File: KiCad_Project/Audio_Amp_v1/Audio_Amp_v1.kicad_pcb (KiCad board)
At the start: 2 copper layers, 93.5 x 52.8 mm, 61 parts, among them IC2 TPA3116D2DAD, IC4 LMR33630ADDA, J1 TS-103-T-A, J2 1729128, J3 1729128, J4 PJ-102AH

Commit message: Started routing
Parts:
- removed CHF1: 220n, Capacitor_SMD:C_0805_2012Metric
- removed CIN1: 10u, Capacitor_SMD:C_1206_3216Metric
- removed IC4: LMR33630ADDA, LMR33630:SOIC127P600X170-9N
- removed J4: PJ-102AH, 24V-JACK:PJ-102AH
- removed L5: IHLP2525CZER6R8M8A, IHLP2525CZER6R8M8A:INDPM6965X300N
- removed R3: 100k, Resistor_SMD:R_0603_1608Metric
- added C30: 10u, Capacitor_SMD:C_0805_2012Metric, F.Cu at (86.8, 96.9)
- added C31: 1u, Capacitor_SMD:C_0603_1608Metric, F.Cu at (101.0, 89.5)
- added C32: 1u, Capacitor_SMD:C_0603_1608Metric, F.Cu at (101.3, 93.1)
- added C33: 1u, Capacitor_SMD:C_0603_1608Metric, F.Cu at (101.3, 96.1)
- added C34: 10u, Capacitor_SMD:C_0603_1608Metric, F.Cu at (101.3, 94.6)
- added C35: 33p, Capacitor_SMD:C_0603_1608Metric, F.Cu at (88.0, 87.9)
- added C36: 33p, Capacitor_SMD:C_0603_1608Metric, F.Cu at (101.0, 87.8)
- added C37: 1u, Capacitor_SMD:C_0603_1608Metric, F.Cu at (88.8, 96.6)
- added C38: 10u, Capacitor_SMD:CP_Elec_4x5.8, F.Cu at (98.0, 101.1)
- added C39: 470u, Capacitor_SMD:CP_Elec_10x10.5, F.Cu at (117.2, 93.0)
- added C40: 10u, Capacitor_SMD:CP_Elec_4x5.8, F.Cu at (91.0, 101.1)
- added C41: 470u, Capacitor_SMD:CP_Elec_10x10.5, F.Cu at (117.5, 120.5)
- added C42: 10u, Capacitor_SMD:C_0805_2012Metric, F.Cu at (79.0, 120.0)
- added C45: 10u, Capacitor_SMD:C_0805_2012Metric, F.Cu at (81.8, 114.2)
- added C50: 100n, Capacitor_SMD:C_0603_1608Metric, F.Cu at (96.8, 122.5)
- added C51: 10u, Capacitor_SMD:C_0805_2012Metric, F.Cu at (96.8, 125.2)
- added C52: 100n, Capacitor_SMD:C_1206_3216Metric, F.Cu at (102.4, 115.5)
- added C53: 100n, Capacitor_SMD:C_1206_3216Metric, F.Cu at (105.2, 115.5)
- added C54: 100n, Capacitor_SMD:C_1206_3216Metric, F.Cu at (87.8, 115.4)
- added C55: 100n, Capacitor_SMD:C_1206_3216Metric, F.Cu at (90.6, 115.4)
- added C56: 10u, Capacitor_SMD:CP_Elec_4x5.8, F.Cu at (100.5, 126.2)
- added C57: 10u, Capacitor_SMD:CP_Elec_4x5.8, F.Cu at (93.0, 126.2)
- added C59: 2n2, Capacitor_SMD:C_0603_1608Metric, F.Cu at (88.3, 121.7)
- added C62: 2n2, Capacitor_SMD:C_0603_1608Metric, F.Cu at (91.3, 121.7)
- added C63: 2n2, Capacitor_SMD:C_0603_1608Metric, F.Cu at (102.3, 121.8)
- added C64: 2n2, Capacitor_SMD:C_0603_1608Metric, F.Cu at (105.3, 121.8)
- added H1: MountingHole_Pad, MountingHole:MountingHole_3.2mm_M3_Pad_Via, F.Cu at (159.0, 82.8)
- added H2: MountingHole_Pad, MountingHole:MountingHole_3.2mm_M3_Pad_Via, F.Cu at (159.0, 135.8)
- added H3: MountingHole_Pad, MountingHole:MountingHole_3.2mm_M3_Pad_Via, F.Cu at (68.0, 135.8)
- added H4: MountingHole_Pad, MountingHole:MountingHole_3.2mm_M3_Pad_Via, F.Cu at (68.0, 82.8)
- added J6: USB_C_Receptacle_USB2.0_16P, Connector_USB:USB_C_Receptacle_GCT_USB4105-xx-A_16P_TopMnt_Horizontal, F.Cu at (66.3, 93.2)
- added Q2: BSS138, Package_TO_SOT_SMD:SOT-23, F.Cu at (106.2, 90.8)
- added R10: 22, Resistor_SMD:R_0603_1608Metric, F.Cu at (87.9, 92.0)
- added R11: 22, Resistor_SMD:R_0603_1608Metric, F.Cu at (87.9, 93.5)
- added R12: 1k, Resistor_SMD:R_0603_1608Metric, F.Cu at (115.8, 102.3)
- added R13: 10k, Resistor_SMD:R_0603_1608Metric, F.Cu at (102.1, 112.2)
- added R14: 1.5k, Resistor_SMD:R_0603_1608Metric, F.Cu at (87.9, 90.5)
- added R16: 1M, Resistor_SMD:R_0603_1608Metric, F.Cu at (94.5, 85.9)
- added R19: 47k, Resistor_SMD:R_0603_1608Metric, F.Cu at (101.5, 101.9)
- added R21: 47k, Resistor_SMD:R_0603_1608Metric, F.Cu at (87.5, 101.9)
- added R22: 10k, Resistor_SMD:R_0603_1608Metric, F.Cu at (105.6, 112.2)
- added R23: 10k, Resistor_SMD:R_0603_1608Metric, F.Cu at (102.9, 118.8)
- added R24: 10k, Resistor_SMD:R_0603_1608Metric, F.Cu at (87.1, 112.2)
- added R25: 3k3, Resistor_SMD:R_0603_1608Metric, F.Cu at (102.9, 120.2)
- added R26: 10k, Resistor_SMD:R_0603_1608Metric, F.Cu at (91.3, 112.2)
- added R27: 10k, Resistor_SMD:R_0603_1608Metric, F.Cu at (90.3, 118.5)
- added R28: 3k3, Resistor_SMD:R_0603_1608Metric, F.Cu at (90.3, 120.0)
- added R29: 100k, Resistor_SMD:R_0603_1608Metric, F.Cu at (82.0, 118.2)
- added R30: 100k, Resistor_SMD:R_0603_1608Metric, F.Cu at (108.0, 93.0)
- added R31: 5k1, Resistor_SMD:R_0603_1608Metric, F.Cu at (72.8, 95.2)
- added R32: 5k1, Resistor_SMD:R_0603_1608Metric, F.Cu at (72.8, 91.2)
- added R33: 100k, Resistor_SMD:R_0603_1608Metric, F.Cu at (79.0, 118.2)
- added RV1: 100k, Potentiometer_THT:Potentiometer_Alps_RK09L_Double_Horizontal, F.Cu at (78.5, 138.3)
- added RV2: 100k, Potentiometer_THT:Potentiometer_Alps_RK09L_Double_Horizontal, F.Cu at (95.8, 138.3)
- added RV3: 10k, Potentiometer_THT:Potentiometer_Alps_RK097_Dual_Horizontal, F.Cu at (113.0, 138.2)
- added U1: PCM2704CDB, PCM2704CDB:SOP65P780X200-28N, F.Cu at (94.5, 92.2)
- added U2: USBLC6-2SC6, Package_TO_SOT_SMD:SOT-23-6, F.Cu at (77.8, 92.7)
- added U3: OPA1678IDR, Package_SO:SOIC-8_3.9x4.9mm_P1.27mm, F.Cu at (96.7, 118.7)
- added U4: L78L12_SOT89, Package_TO_SOT_SMD:SOT-89-3, F.Cu at (80.8, 110.5)
- added XC1: 12Mhz, Crystal:Crystal_SMD_HC49-SD, F.Cu at (94.5, 82.1)
- C1, C2, C4, C5: value 1u -> 3u3
- C43: value 1u -> 0.33u; footprint Capacitor_SMD:C_0603_1608Metric -> PCM_JLCPCB:C_0805
- C44: value 100n -> 0.1u
- C46: value 22u -> 4u7
- C47: value 22u -> 47u; footprint Capacitor_SMD:C_0805_2012Metric -> Capacitor_SMD:CP_Elec_6.3x5.9
- C48, C49: value 22u -> 10u; footprint Capacitor_SMD:C_0805_2012Metric -> Capacitor_SMD:CP_Elec_4x5.8
- J1: value TS-103-T-A -> Screw_Terminal_01x02; footprint TS_103_T_A:SAMTEC_TS-103-T-A -> TerminalBlock_Phoenix:TerminalBlock_Phoenix_MKDS-1,5-2-5.08_1x02_P5.08mm_Horizontal
- J2: value 1729128 -> Screw_Terminal_01x02; footprint Phoenix-1729128:1729128 -> TerminalBlock_Phoenix:TerminalBlock_Phoenix_MKDS-1,5-2-5.08_1x02_P5.08mm_Horizontal
- J3: value 1729128 -> Barrel_Jack_Switch; footprint Phoenix-1729128:1729128 -> Connector_BarrelJack:BarrelJack_CUI_PJ-102AH_Horizontal
- R17: value 100k -> 47k
- R20: value 43.2k -> 10k
- moved J3 81.6 mm to (75.8, 108.8)
- moved J1 66.5 mm to (161.9, 102.0), turned to 90 degrees
- moved TP3 57.2 mm to (146.0, 88.5)
- moved TP4 43.6 mm to (141.8, 88.5)
- moved C44 34.5 mm to (82.0, 116.2), turned to 180 degrees
- moved C43 27.2 mm to (82.0, 106.8), turned to 180 degrees
- moved C47 27.0 mm to (109.8, 102.3), turned to 0 degrees
- moved J2 23.5 mm to (161.9, 120.5), turned to 90 degrees
- moved C46 22.7 mm to (106.2, 94.2)
- moved C48 21.2 mm to (99.3, 107.1), turned to 180 degrees
- moved C49 18.4 mm to (90.2, 107.1), turned to 0 degrees
- moved C17 14.9 mm to (130.5, 124.2), turned to 180 degrees
- moved C10 13.8 mm to (130.5, 91.0), turned to 0 degrees
- moved C8 13.7 mm to (130.3, 103.2), turned to 180 degrees
- moved C9 10.9 mm to (130.3, 101.2), turned to 180 degrees
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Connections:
- C10 pad 2: IN_COM -> GNDA
- C15 pad 2: IN_COM -> GNDA
- C16 pad 2: IN_COM -> GNDA
- C17 pad 2: IN_COM -> GNDA
- C18 pad 2: IN_COM -> GNDA
- C19 pad 1: IN_COM -> GNDA
- C2 pad 1: IN_COM -> GNDA
- C20 pad 2: IN_COM -> GNDA
- C21 pad 1: IN_COM -> GNDA
- C22 pad 1: IN_COM -> GNDA
- C23 pad 2: IN_COM -> GNDA
- C24 pad 2: IN_COM -> GNDA
- C25 pad 1: IN_COM -> GNDA
- C26 pad 2: IN_COM -> GNDA
- C27 pad 1: IN_COM -> GNDA
- C28 pad 2: IN_COM -> GNDA
- C29 pad 1: IN_COM -> GNDA
- C3 pad 1: IN_COM -> GNDA
- C43 pad 1: Net-(IC4-VCC) -> +24V
- C43 pad 2: IN_COM -> GNDA
- C44 pad 1: Net-(IC4-BOOT) -> +12V
- C44 pad 2: Net-(IC4-SW) -> GNDA
- C46 pad 1: IN_COM -> MUTE
- C46 pad 2: +3.3V -> GNDA
- C47 pad 1: IN_COM -> GNDA
- C47 pad 2: +3.3V -> Net-(IC2-SDZ)
- C48 pad 1: IN_COM -> Net-(C48-Pad1)
- C48 pad 2: +3.3V -> DAC_L
- C49 pad 1: IN_COM -> Net-(C49-Pad1)
- C49 pad 2: +3.3V -> DAC_R
- C5 pad 2: IN_COM -> GNDA
- C6 pad 1: IN_COM -> GNDA
- C7 pad 1: IN_COM -> GNDA
- C8 pad 2: IN_COM -> GNDA
- C9 pad 2: IN_COM -> GNDA
- IC2 pad 1: IN_COM -> GNDA
- IC2 pad 12: Net-(IC2-MUTE) -> MUTE
- IC2 pad 13: IN_COM -> GNDA
- IC2 pad 14: IN_COM -> GNDA
- IC2 pad 15: IN_COM -> GNDA
- IC2 pad 2: Net-(IC2-FAULTZ) -> Net-(IC2-SDZ)
- IC2 pad 22: IN_COM -> GNDA
- IC2 pad 25: IN_COM -> GNDA
- IC2 pad 28: IN_COM -> GNDA
- IC2 pad 33: IN_COM -> GNDA
- IC2 pad 9: IN_COM -> GNDA
- J2 pad 1: OUT_P_RIGHT -> OUT_N_LEFT
- J2 pad 2: OUT_N_RIGHT -> OUT_P_LEFT
- J3 pad 1: OUT_P_LEFT -> +24V
- J3 pad 2: OUT_N_LEFT -> GNDA
- R17 pad 1: Net-(IC4-FB) -> Net-(Q2-D)
- R17 pad 2: +3.3V -> +12V
- R2 pad 2: IN_COM -> GNDA
- R20 pad 1: IN_COM -> GNDA
- R20 pad 2: Net-(IC4-FB) -> /USB_DAC/DAC_ACTIVE
- R4 pad 2: Net-(IC2-FAULTZ) -> Net-(IC2-SDZ)
- TP3 pad 1: +3.3V -> +12V
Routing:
- net +24V: track 107.2 -> 9.41 mm, vias 25 -> 0
- net IN_COM: track 68.1 -> 0.00 mm, vias 79 -> 0
- net Net-(C52-Pad2): track 0.00 -> 60.4 mm
- net Net-(C52-Pad1): track 0.00 -> 57.7 mm, vias 0 -> 2
- net Net-(C53-Pad2): track 0.00 -> 57.0 mm, vias 0 -> 1
- net +3.3V: track 46.2 -> 0.00 mm, vias 16 -> 0
- net Net-(C55-Pad2): track 0.00 -> 35.4 mm
- net OUT_N_RIGHT: track 35.0 -> 0.00 mm
- net OUT_P_RIGHT: track 34.4 -> 0.00 mm
- net OUT_N_LEFT: track 34.0 -> 0.00 mm
- net OUT_P_LEFT: track 34.0 -> 0.00 mm
- net Net-(C64-Pad2): track 0.00 -> 32.3 mm, vias 0 -> 1
- net Net-(C57-Pad2): track 0.00 -> 31.3 mm, vias 0 -> 1
- net Net-(C54-Pad1): track 0.00 -> 31.3 mm, vias 0 -> 1
- net Net-(C54-Pad2): track 0.00 -> 29.1 mm, vias 0 -> 1
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- removed copper zone on F.Cu, net +24V
- removed copper zone on F.Cu, net +3.3V
- removed copper zone on B.Cu, net IN_COM
- removed copper zone on F.Cu, net IN_COM
- removed copper zone on F.Cu, net Net-(IC4-SW)
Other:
- board size 93.5 x 52.8 mm -> 102 x 64 mm
- copper layers 2 -> 4
- board text added: "USB-C Class-D Amp - v1.0"

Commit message: layout finished
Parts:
- moved TP3 31.0 mm to (115.2, 84.8)
- moved TP4 22.3 mm to (119.8, 84.8)
- moved C15 5.15 mm to (125.4, 115.4), turned to 180 degrees
- moved C14 3.54 mm to (129.8, 112.6)
- moved C42 2.00 mm to (79.0, 122.0)
- moved C44 2.00 mm to (82.0, 118.2)
- moved C45 2.00 mm to (81.8, 116.2)
- moved J3 2.00 mm to (75.8, 110.8)
- moved R29 2.00 mm to (82.0, 120.2)
- moved R33 2.00 mm to (79.0, 120.2)
- moved U4 2.00 mm to (80.8, 112.5)
- moved C43 1.46 mm to (82.8, 108.0), turned to 90 degrees
- moved C13 0.53 mm to (129.8, 109.2), turned to -90 degrees
- moved C8 0.42 mm to (130.3, 102.8)
- moved C9 0.42 mm to (130.3, 100.8)
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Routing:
- net GNDA: track 6.77 -> 124.9 mm, vias 0 -> 61
- net IN_P_RIGHT: track 0.00 -> 37.3 mm
- net +12V: track 9.84 -> 46.6 mm, vias 0 -> 11
- net IN_P_LEFT: track 0.00 -> 28.9 mm
- net MUTE: track 2.86 -> 31.4 mm, vias 0 -> 2
- net VBUS: track 5.15 -> 29.4 mm, vias 0 -> 3
- net /Tone-Volume_control/VREF: track 5.48 -> 27.3 mm, vias 0 -> 2
- net Net-(IC2-OUTPR): track 2.73 -> 19.2 mm
- net Net-(IC2-OUTNL): track 5.81 -> 21.1 mm
- net Net-(IC2-OUTPL): track 2.60 -> 13.9 mm
- net Net-(IC2-OUTNR): track 5.81 -> 14.3 mm
- net Net-(C49-Pad1): track 10.0 -> 16.0 mm
- net Net-(IC2-BSPR): track 4.92 -> 10.4 mm, vias 0 -> 2
- net Net-(IC2-BSNR): track 6.20 -> 11.2 mm, vias 0 -> 2
- net Net-(IC2-BSNL): track 6.14 -> 11.0 mm, vias 0 -> 2
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- added copper zone on F.Cu, net +12V
- added copper zone on In2.Cu, net +12V
- added copper zone on F.Cu, net +24V
- added copper zone on In2.Cu, net +24V
- added copper zone on F.Cu, net GNDA
- added copper zone on In1.Cu, net GNDA
- added copper zone on F.Cu, net Net-(IC2-SDZ)
- added copper zone on F.Cu, net OUT_N_LEFT
- added copper zone on F.Cu, net OUT_N_RIGHT
- added copper zone on F.Cu, net OUT_P_LEFT
- added copper zone on F.Cu, net OUT_P_RIGHT
- added copper zone on F.Cu, net VBUS

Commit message: added reverse polarity protection
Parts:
- added D1: D_Zener, Diode_SMD:D_SOD-123, F.Cu at (78.2, 106.6)
- added F1: Fuse, Fuse:Fuse_2920_7451Metric_Pad2.10x5.45mm_HandSolder, F.Cu at (70.2, 113.6)
- added Q1: Q_PMOS_GDS, Package_TO_SOT_SMD:TO-252-2, F.Cu at (70.2, 106.7)
- added R34: 47k, Resistor_SMD:R_0603_1608Metric, F.Cu at (77.0, 112.2)
- moved J3 11.5 mm to (73.8, 122.0)
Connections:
- C1 pad 1: IN_P_RIGHT -> GNDA
- C2 pad 1: GNDA -> IN_P_RIGHT
- C4 pad 2: IN_P_LEFT -> GNDA
- C5 pad 2: GNDA -> IN_P_LEFT
- J3 pad 1: +24V -> +24VIN
- RV1 pad MP: (no net) -> GNDA
- RV2 pad MP: (no net) -> GNDA
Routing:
- net Net-(IC2-OUTNL): track 21.1 -> 3.48 mm
- net Net-(IC2-OUTPR): track 19.2 -> 2.94 mm
- net Net-(IC2-OUTPL): track 13.9 -> 3.43 mm
- net IN_P_LEFT: track 28.9 -> 35.8 mm
- net Net-(IC2-OUTNR): track 14.3 -> 8.09 mm
- net Net-(D1-A): track 0.00 -> 5.86 mm
- net GNDA: track 124.9 -> 123.6 mm, vias 61 -> 63
- net IN_P_RIGHT: track 37.3 -> 36.0 mm
- net Net-(IC2-GVDD): track 4.67 -> 5.79 mm
- net +24V: vias 62 -> 75
- added copper zone on F.Cu, net +24VIN
- added copper zone on F.Cu, net Net-(IC2-OUTNL)
- added copper zone on F.Cu, net Net-(IC2-OUTNR)
- added copper zone on F.Cu, net Net-(IC2-OUTPL)
- added copper zone on F.Cu, net Net-(IC2-OUTPR)
- added copper zone on F.Cu, net Net-(Q1-D)

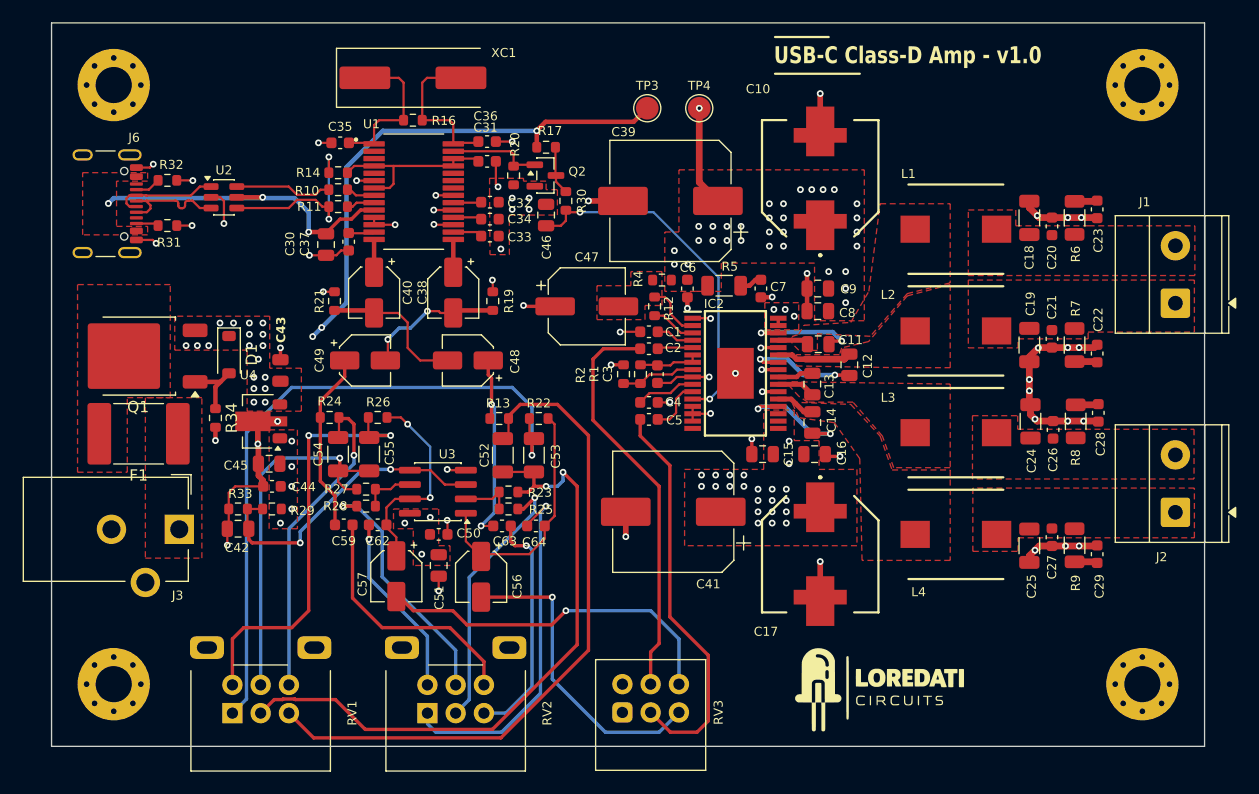
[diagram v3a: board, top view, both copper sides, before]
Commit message: Added led into pcb and lyout completed
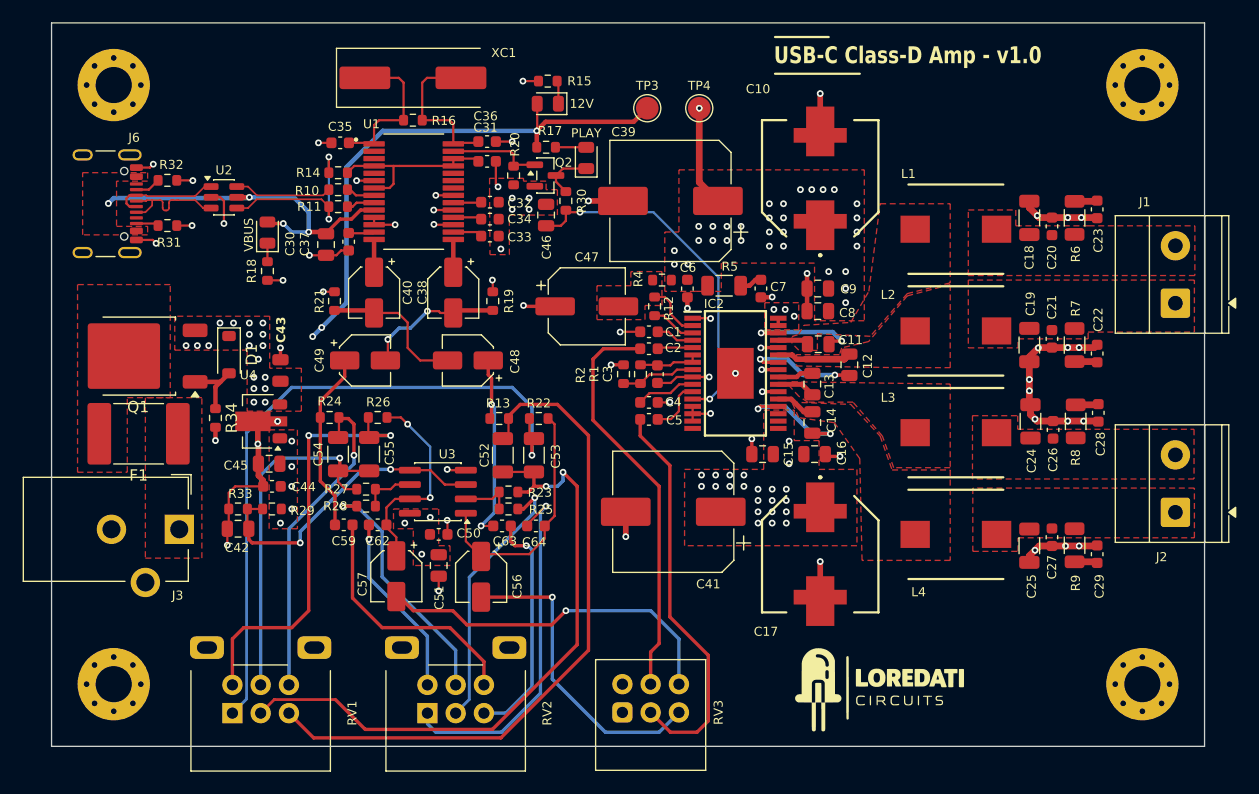
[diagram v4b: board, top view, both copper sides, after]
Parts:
- added 12V: LED, LED_SMD:LED_0805_2012Metric, F.Cu at (106.4, 84.4)
- added PLAY: LED, LED_SMD:LED_0805_2012Metric, F.Cu at (109.8, 89.2)
- added R15: 3k3, Resistor_SMD:R_0603_1608Metric, F.Cu at (106.4, 82.4)
- added R18: 1k, Resistor_SMD:R_0603_1608Metric, F.Cu at (81.6, 99.2)
- added VBUS: LED, LED_SMD:LED_0805_2012Metric, F.Cu at (81.6, 95.8)
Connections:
- Q2 pad 3: Net-(Q2-D) -> Net-(D4-K)
- R17 pad 1: Net-(Q2-D) -> Net-(D4-A)
- R30 pad 2: Net-(Q2-D) -> Net-(D4-K)
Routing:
- net Net-(D4-K): track 0.00 -> 4.39 mm
- net Net-(Q2-D): track 4.31 -> 0.00 mm
- net Net-(D4-A): track 0.00 -> 3.13 mm
- net VBUS: track 29.3 -> 32.2 mm, vias 3 -> 4
- net GNDA: track 123.6 -> 126.4 mm, vias 63 -> 65
- net +12V: track 46.6 -> 49.0 mm
- net Net-(D2-K): track 0.00 -> 2.05 mm
- net Net-(D3-K): track 0.00 -> 1.64 mm
- net /USB_DAC/USB_D+: track 9.99 -> 10.8 mm
